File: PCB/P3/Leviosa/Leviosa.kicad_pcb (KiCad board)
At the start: 2 copper layers, 80 x 80 mm, 59 parts, among them J1 Barrel_Jack, J2 2.54mm 1x03 Spare, Q1 NCE0110K, U1 TPS1H200AQDGNRQ1, U2 MC7805BD2TR4G, U3 SS495A, U4 MCP6001R, U5 LM393, U6 MX27517, U7 INA199xxDCK (50V/V)

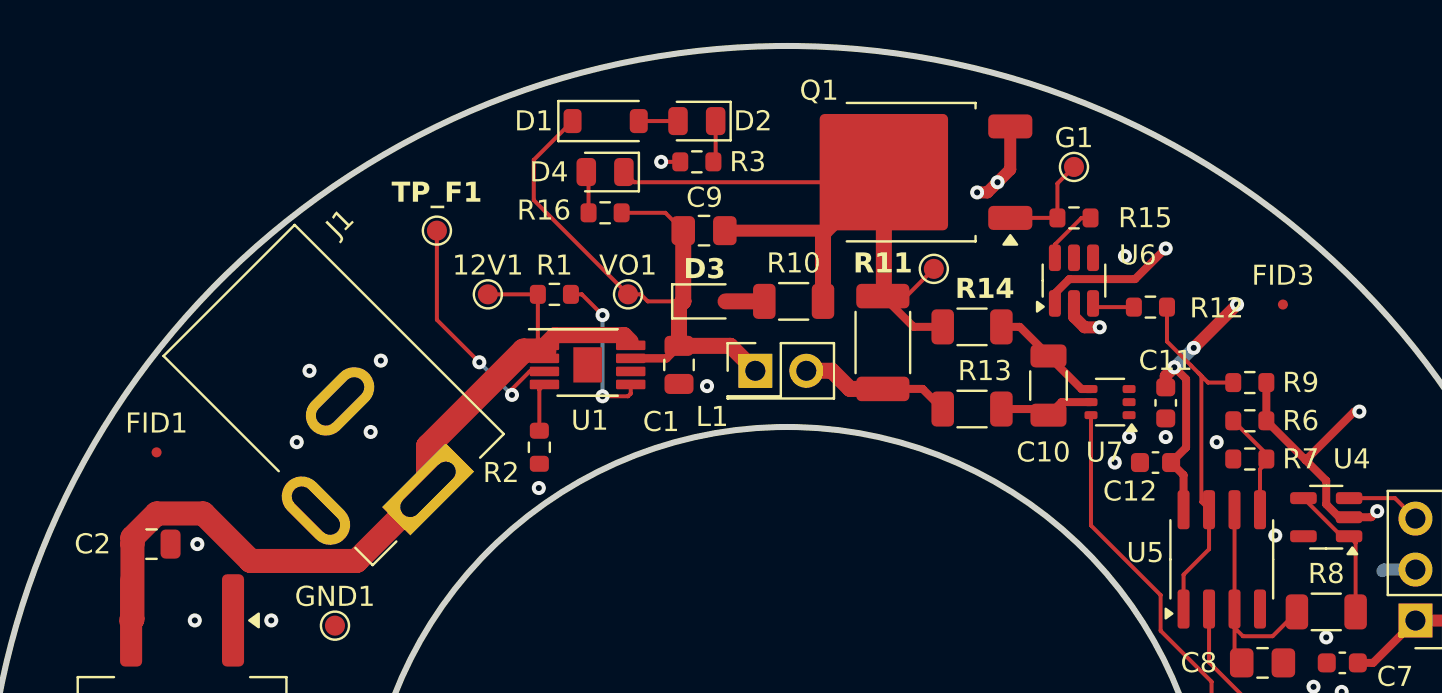
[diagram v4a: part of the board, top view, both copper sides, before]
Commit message: add 0.1uF cap to gate driver VCC
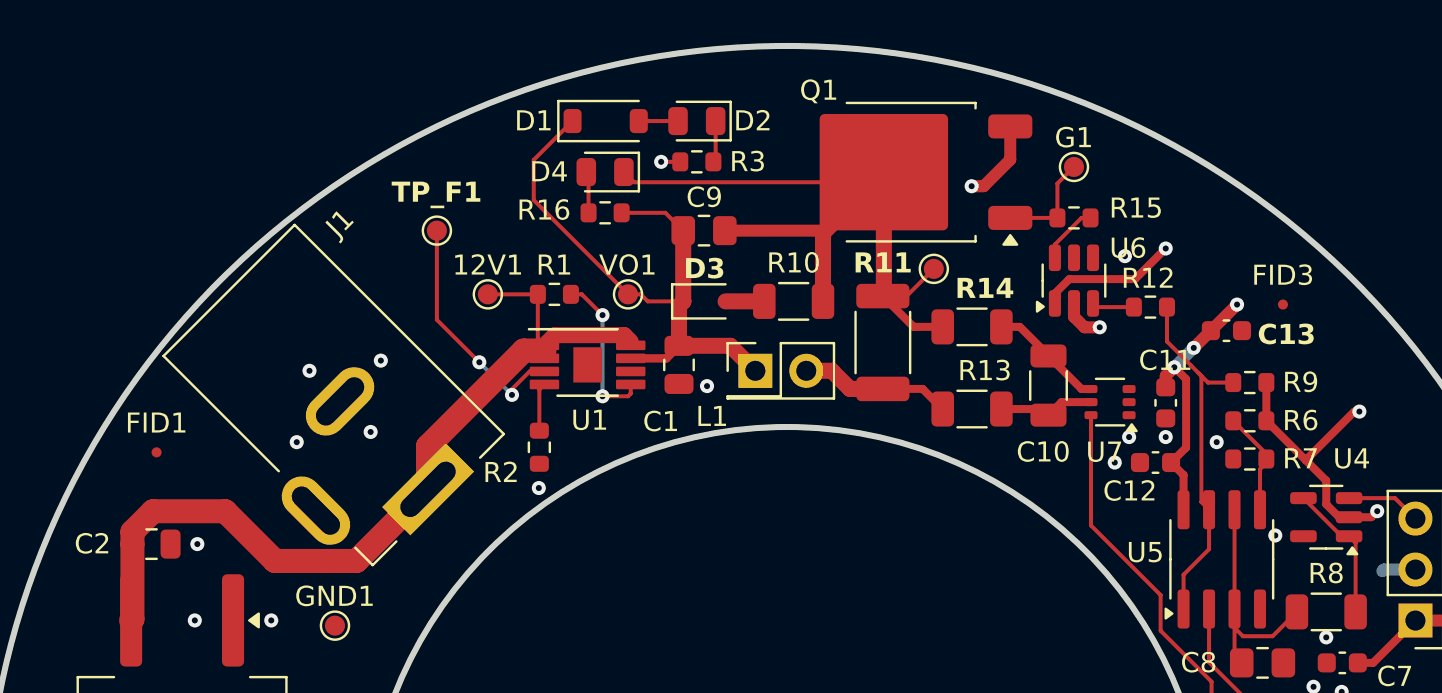
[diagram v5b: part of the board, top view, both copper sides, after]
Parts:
- added C13: 0.1uF, Capacitor_SMD:C_0603_1608Metric, F.Cu at (121.9, 74.2)
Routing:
- net GND: track 10.2 -> 10.1 mm, vias 27 -> 26

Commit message: update H1 pos
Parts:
- moved H1 0.54 mm to (110.0, 125.0)
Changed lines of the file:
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@@
 	(footprint "MountingHole:MountingHole_3.2mm_M3_ISO7380"
 		(layer "F.Cu")
-		(at 109.982 124.46)
+		(at 110 125)
 		(descr "Mounting Hole 3.2mm, M3, no annular, generated by kicad-footprint-generator mountinghole.py")
 		(tags "mountinghole M3 ISO7380")

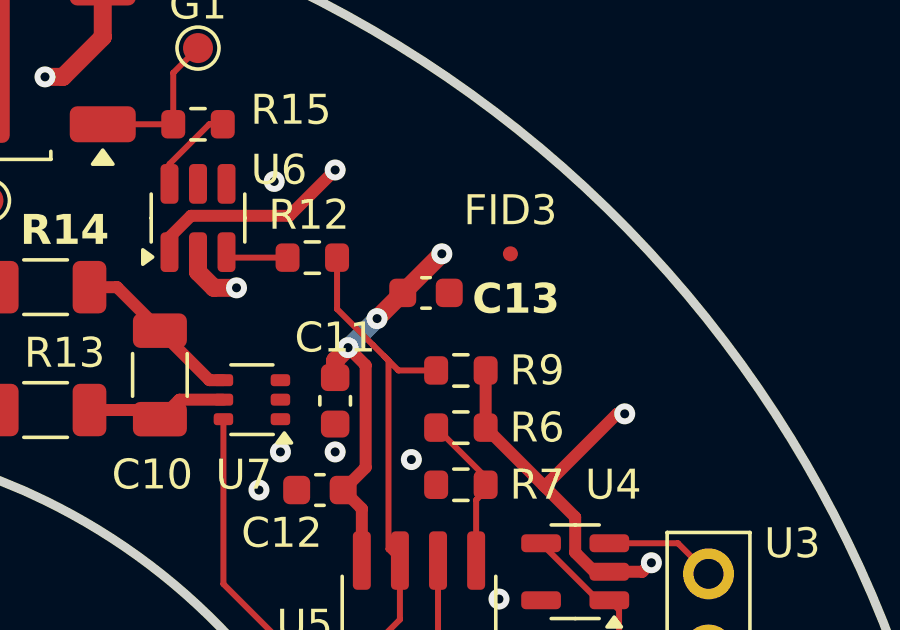
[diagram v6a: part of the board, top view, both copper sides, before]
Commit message: add via
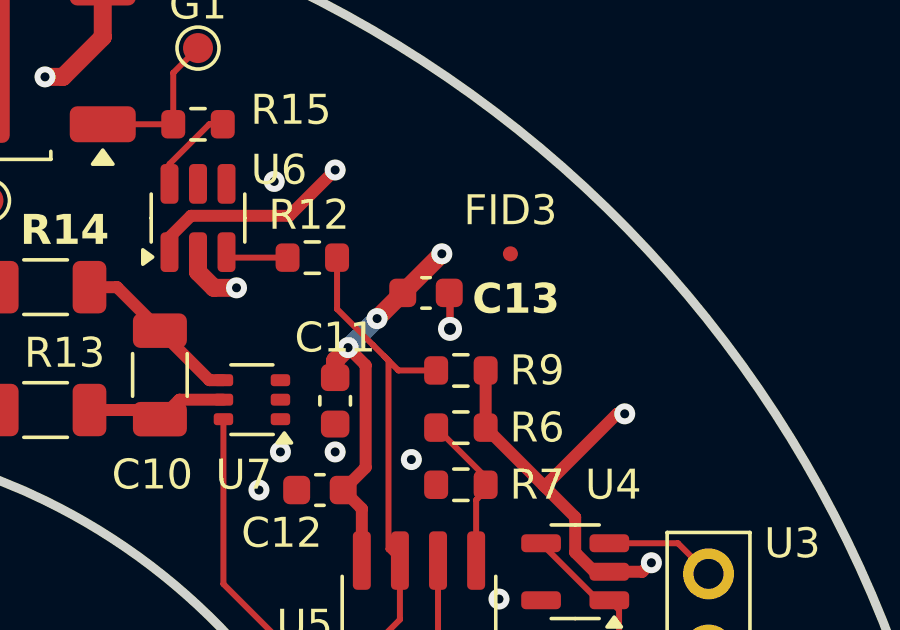
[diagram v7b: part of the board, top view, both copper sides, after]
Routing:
- net GND: track 10.1 -> 11.3 mm, vias 26 -> 27
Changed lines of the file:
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@@
+	)
+	(segment
+		(start 122.7 75.4)
+		(end 122.7 74.225)
+		(width 0.25)
+		(layer "F.Cu")
+		(net 2)
+	)
+	(segment
+		(start 122.7 74.225)
+		(end 122.675 74.2)
+		(width 0.25)
+		(layer "F.Cu")
+		(net 2)
 	)
 	(segment
@@
 		(layers "F.Cu" "B.Cu")
 		(free yes)
+		(net 2)
+	)
+	(via
+		(at 122.7 75.4)
+		(size 0.8)
+		(drill 0.4)
+		(layers "F.Cu" "B.Cu")
+		(free yes)

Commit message: gerbers created
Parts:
- removed D1: BZT52C8V2 WD, Diode_SMD:D_SOD-123
- R3: value 1kΩ -> 2kΩ
- U1: footprint TPS1H200AQDGNRQ1:SOP65P490X110-9N -> Package_SO:HVSSOP-8-1EP_3x3mm_P0.65mm_EP1.57x1.89mm
- moved R1 6.98 mm to (90.7, 79.0)
- moved D2 3.37 mm to (92.1, 64.0)
- moved R3 1.83 mm to (95.9, 64.0), turned to 0 degrees
- moved D4 1.21 mm to (92.1, 66.3)
- moved R16 1.21 mm to (92.1, 68.3)
- moved C1 0.64 mm to (95.2, 75.9)
- moved U1 0.55 mm to (90.6, 75.9)
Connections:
- D2 pad 2: Net-(D1-A) -> +12V_SF
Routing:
- net +12V: track 41.8 -> 49.6 mm
- net Net-(U1-DELAY): track 7.97 -> 2.69 mm, vias 2 -> 0
- net GND: track 11.3 -> 15.7 mm, vias 27 -> 29
- net +12V_SF: track 30.5 -> 28.0 mm
- net Net-(D1-A): track 1.95 -> 0.00 mm
- net +5V: track 84.9 -> 86.7 mm
- net /COIL_OUT: track 43.1 -> 41.5 mm
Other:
- board text added: "COIL"
- board text added: "December 10th 2025"
- board text added: "PWR"
- board text added: "V4"
